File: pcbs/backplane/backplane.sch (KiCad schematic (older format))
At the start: 49 parts, among them P1 USB_B, P3 CONN_02X03, P4 CONN_02X03, P5 CONN_02X07, P6 CONN_02X07, P7 CONN_01X03, P8 CONN_01X03, Q1 MMBT3904, Q2 MMBT3904, Q3 Si2323, U1 LM358, U2 TC1262-33VDB, U3 LM358, U4 CH340G, Y1 Crystal

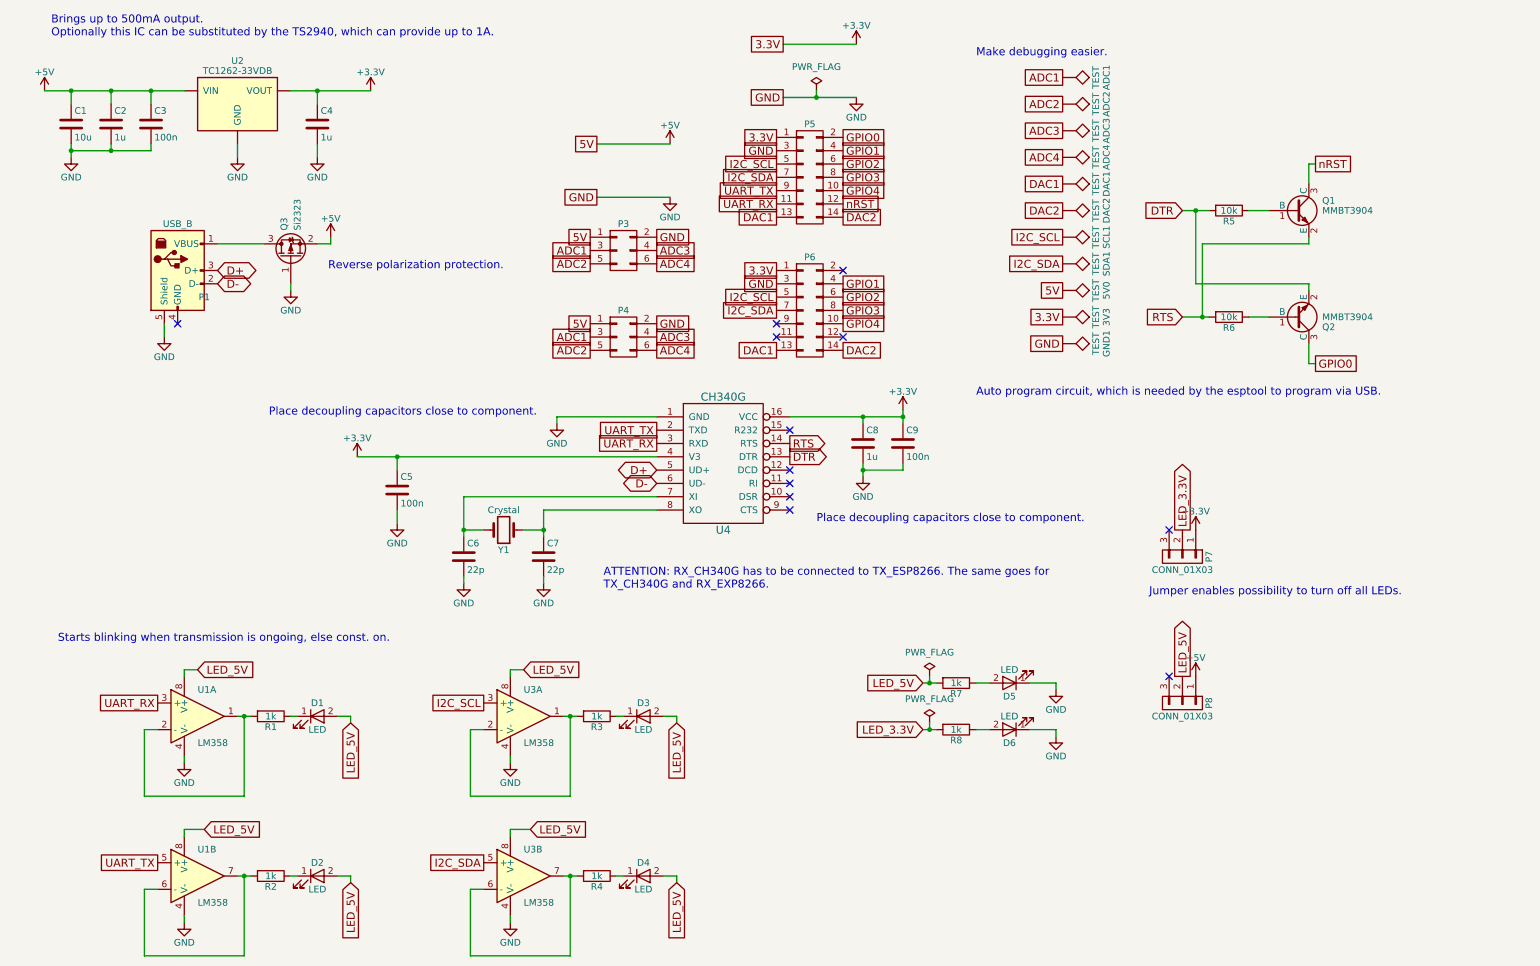
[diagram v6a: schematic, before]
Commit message: Small changes on the backplane standing out.
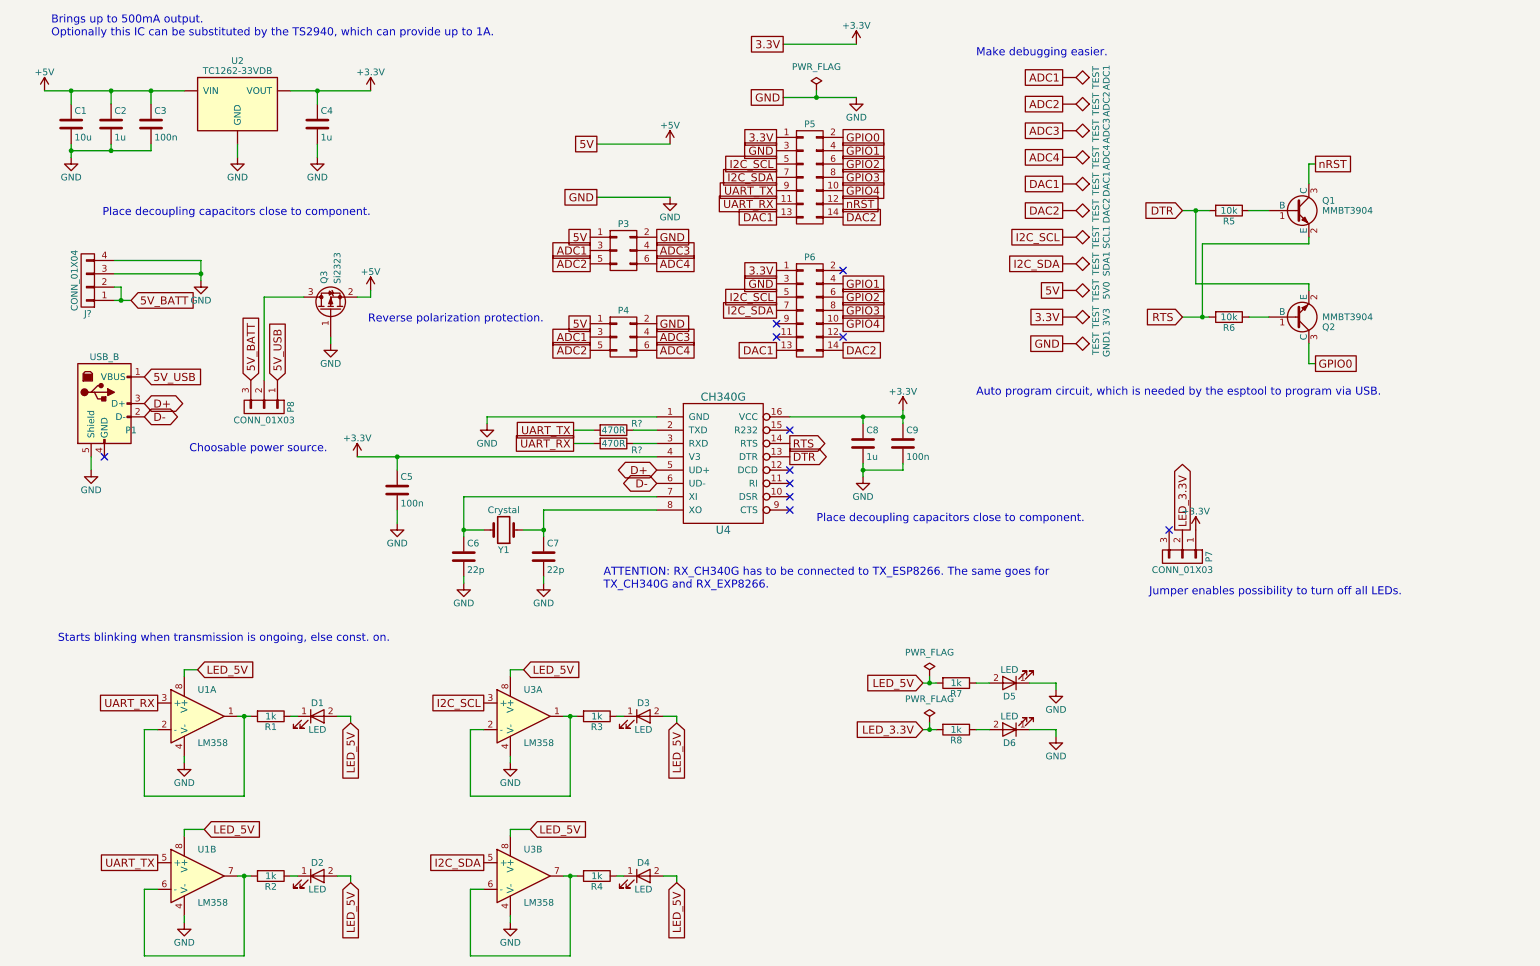
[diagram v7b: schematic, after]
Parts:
- added J?: CONN_01X04, ConnectorsChina:LED_CONN_1.25_PITCH, symbol CONN_01X04
- added R? (x2): 470R, Resistors_SMD:R_0805, symbol R
- P3, P4: Samtec (none) -> TSW-103-08-G-D-RA
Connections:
- net +5V: no longer P8.1 (P1)
- net GND: now also J?.3 (P3), J?.4 (P4)
- net LED_5V: no longer P8.2 (P2)
- net UART_RX: now also R?.2; no longer U4.3 (RXD)
- net UART_TX: now also R?.2; no longer U4.2 (TXD)
- net at Q3.3 (D): now also P8.2 (P2); no longer P1.1 (VBUS)
- net 5V_BATT: now reaches P8.3 (P3)
- net 5V_BATT: now also J?.1 (P1), J?.2 (P2)
- new net: R?.1, U4.2 (TXD)
- new net: R?.1, U4.3 (RXD)
- new net 5V_USB: P1.1 (VBUS), P8.1 (P1)
- no-connect marks 12 -> 11
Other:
- note added: "Choosable power source."
- moved on the sheet: P1, P8, Q3

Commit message: Backplane definitely finished. Somethings wrong with TIA. Has to be checked tomorrow.
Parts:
- added C10, C11: 10u, Resistors_SMD:R_0805, symbol C
- added C12, C13: 100n, Resistors_SMD:R_0805, symbol C
- added P2: CONN_01X03, mySamtec:Samtec-PHT-1-3-01-L-S, symbol CONN_01X03
- P3, P4: Samtec TSW-103-08-G-D-RA -> BCS-103-F-D-TE
- gave numbers to parts that had none: 3
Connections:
- net +5V: now also P2.1 (P1)
- net GND: now also C10.2, C11.2, C12.2, C13.2
- net LED_5V: now also C10.1, C11.1, C12.1, C13.1, P2.2 (P2)
- no-connect marks 11 -> 12
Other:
- moved on the sheet: P7
